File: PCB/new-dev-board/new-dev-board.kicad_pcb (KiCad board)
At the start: 2 copper layers, 185 x 135 mm, 4 parts, among them J1 SIM7600

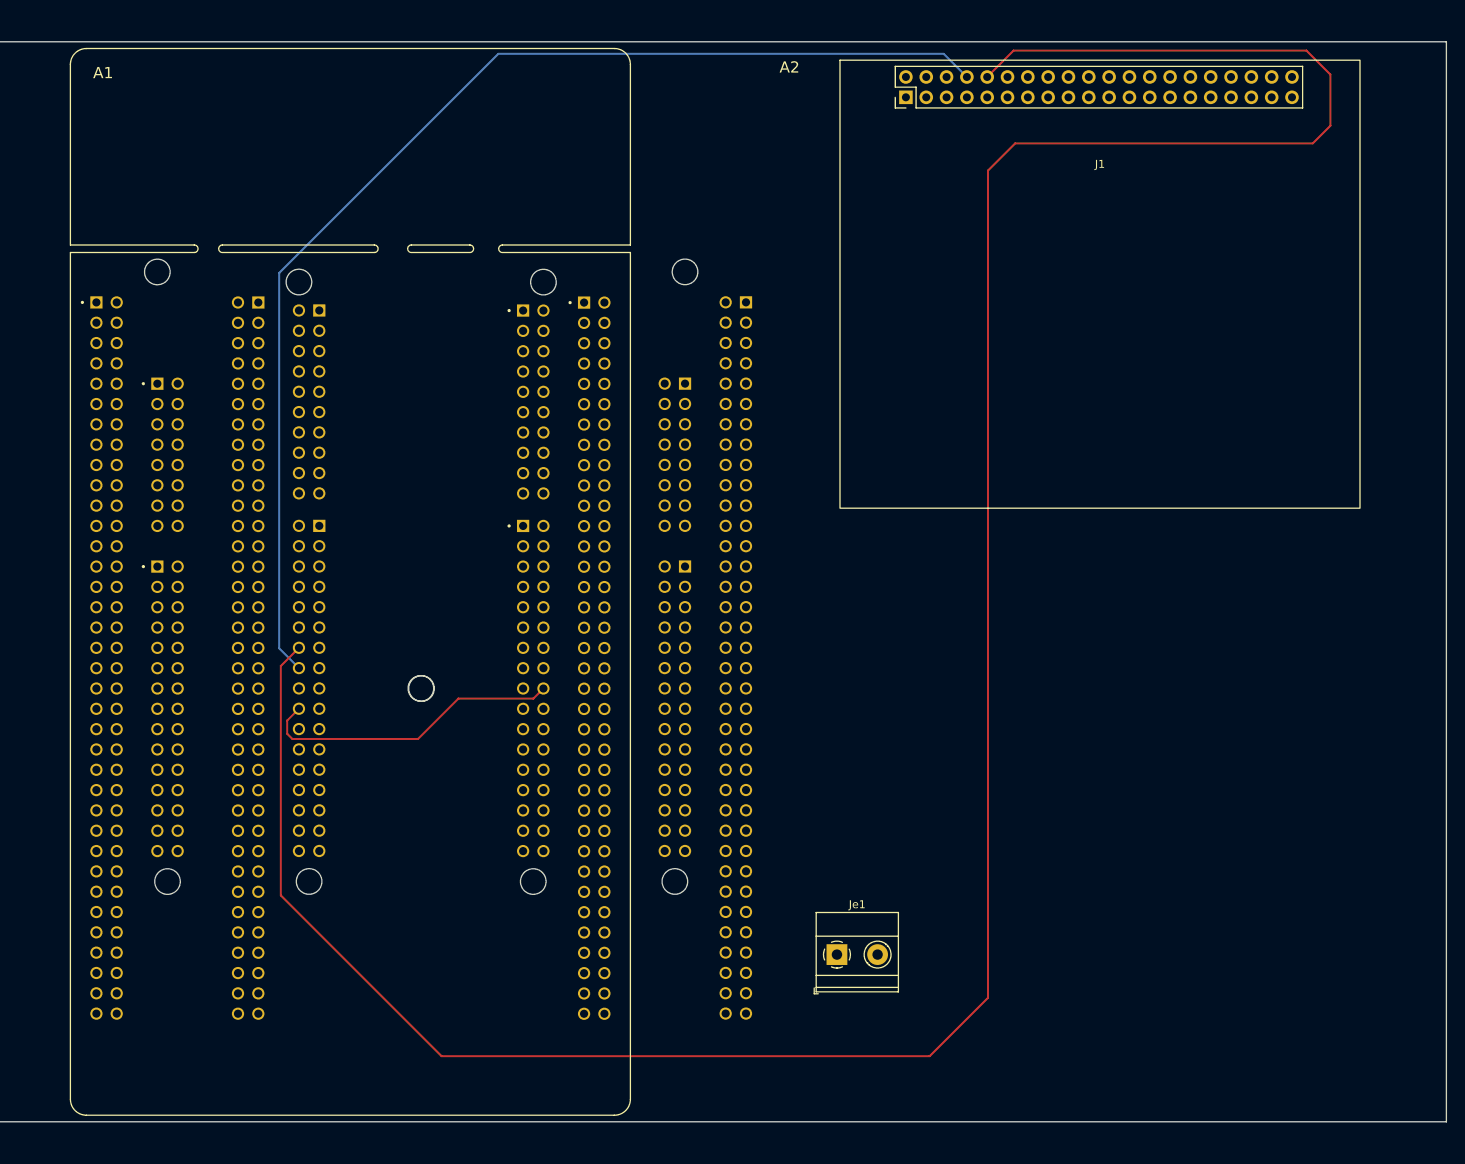
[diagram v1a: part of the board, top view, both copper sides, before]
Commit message: added 2 mount holes
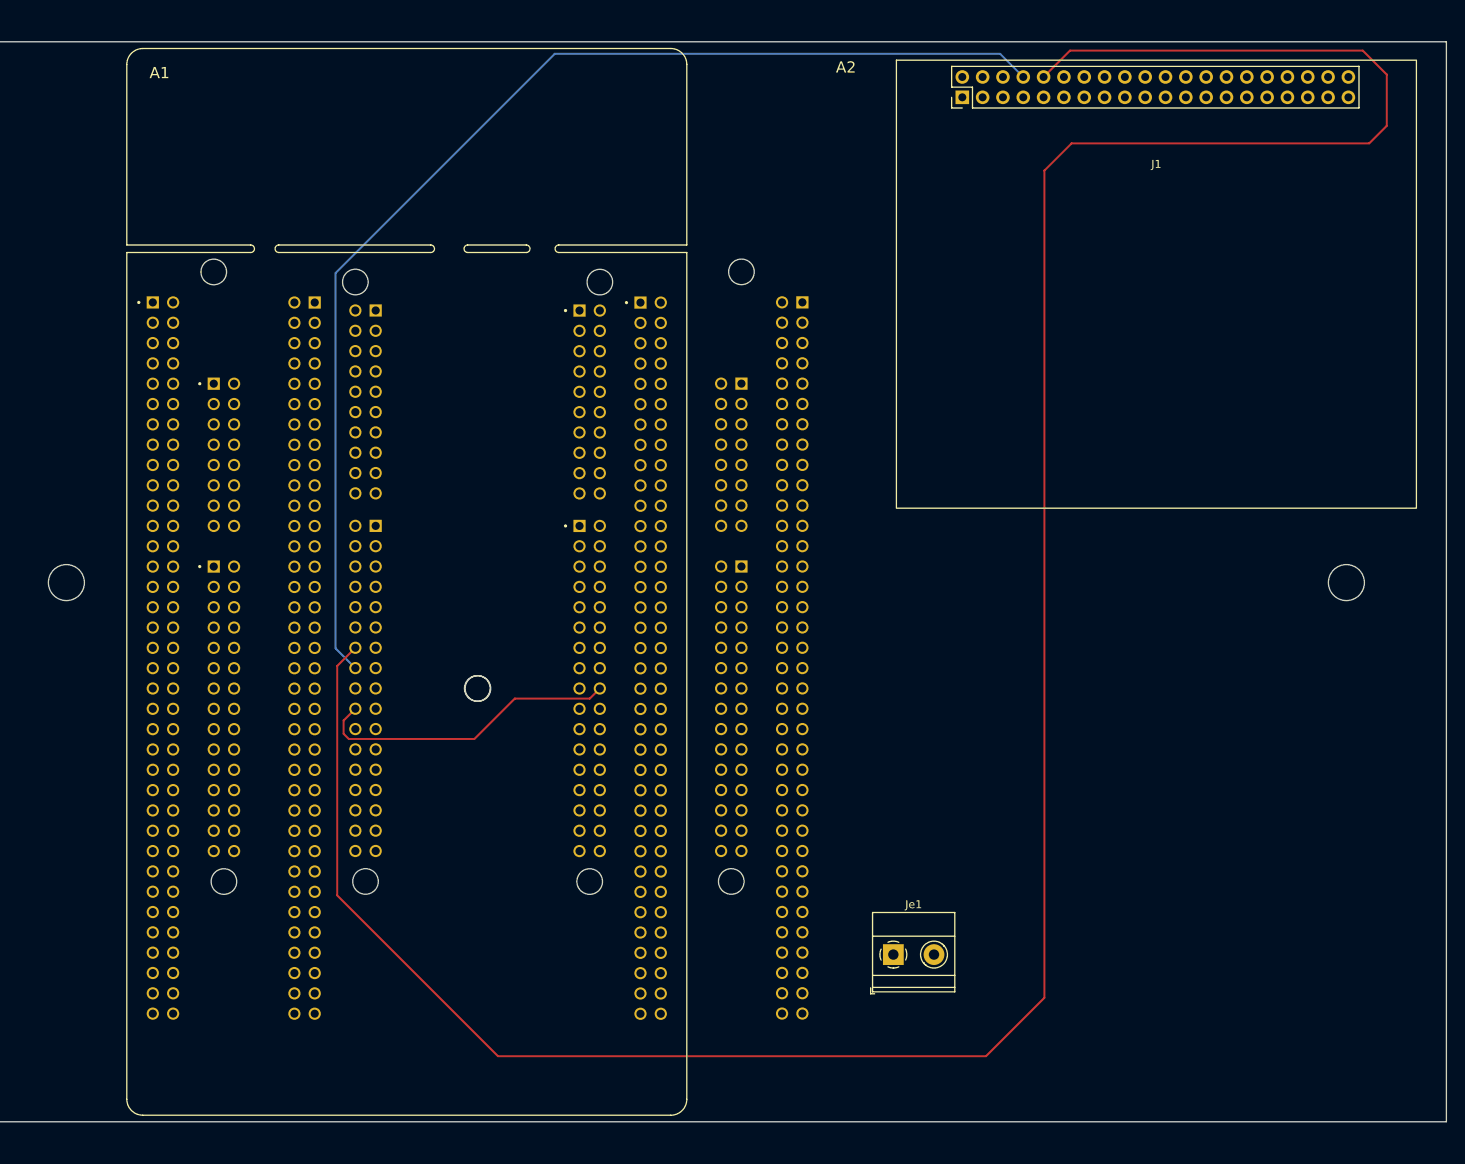
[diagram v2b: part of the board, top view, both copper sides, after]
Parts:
- moved J1 7.05 mm to (201.2, 50.1)
- moved Je1 7.05 mm to (168.4, 133.9)
- moved A1 7.05 mm to (107.5, 87.3)
- moved A2 7.05 mm to (125.2, 87.3)
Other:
- outline, holes or cut-outs redrawn
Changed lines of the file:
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@@
       (drillshape 0)
       (scaleselection 1)
-      (outputdirectory "gerber files/")
+      (outputdirectory "gerber files/first_try/")
     )
   )
@@
   (net 477 "unconnected-(J1-Pin_40-Pad40)")
   (footprint "NUCLEO-F767ZI:SIM7600" (layer "F.Cu")
-    (at 194.2 50.1)
+    (at 201.25 50.1)
     (property "Sheetfile" "new-dev-board.kicad_sch")
     (property "Sheetname" "")
@@
   )
   (footprint "TerminalBlock_Phoenix:TerminalBlock_Phoenix_MKDS-1,5-2-5.08_1x02_P5.08mm_Horizontal" (layer "F.Cu")
-    (at 161.32 133.9)
+    (at 168.37 133.9)
     (descr "Terminal Block Phoenix MKDS-1,5-2-5.08, 2 pins, pitch 5.08mm, size 10.2x9.8mm^2, drill diamater 1.3mm, pad diameter 2.6mm, see http://www.farnell.com/datasheets/100425.pdf, script-generated using https://github.com/pointhi/kicad-footprint-generator/scripts/TerminalBlock_Phoenix")
     (tags "THT Terminal Block Phoenix MKDS-1,5-2-5.08 pitch 5.08mm size 10.2x9.8mm^2 drill 1.3mm pad 2.6mm")
@@
   )
   (footprint "NUCLEO-F767ZI:NUCLEO-F767ZI" (layer "F.Cu")
-    (at 100.5 87.31)
+    (at 107.55 87.31)
     (property "MANUFACTURER" "STMicroelectronics")
     (property "MAXIMUM_PACKAGE_HEIGHT" "N/A")
@@
   )
   (footprint "NUCLEO-F767ZI:NUCLEO-F767ZI" (layer "B.Cu")
-    (at 118.2 87.3 180)
+    (at 125.25 87.3 180)
     (property "MANUFACTURER" "STMicroelectronics")
     (property "MAXIMUM_PACKAGE_HEIGHT" "N/A")
@@
   (gr_rect (start 52.5 19.8) (end 237.5 154.8)
     (stroke (width 0.1) (type default)) (fill none) (layer "Edge.Cuts"))
-  (segment (start 123.37 101.9) (end 114 101.9) (width 0.25) (layer "F.Cu") (net 124))
-  (segment (start 92.6 106.3) (end 92.6 104.64) (width 0.25) (layer "F.Cu") (net 124))
-  (segment (start 124.63 100.64) (end 123.37 101.9) (width 0.25) (layer "F.Cu") (net 124))
-  (segment (start 108.95 106.95) (end 93.25 106.95) (width 0.25) (layer "F.Cu") (net 124))
-  (segment (start 93.25 106.95) (end 92.6 106.3) (width 0.25) (layer "F.Cu") (net 124))
-  (segment (start 92.6 104.64) (end 94.07 103.17) (width 0.25) (layer "F.Cu") (net 124))
-  (segment (start 114 101.9) (end 108.95 106.95) (width 0.25) (layer "F.Cu") (net 124))
-  (segment (start 223 23.9) (end 220 20.9) (width 0.25) (layer "F.Cu") (net 341))
-  (segment (start 223 30.3) (end 223 23.9) (width 0.25) (layer "F.Cu") (net 341))
-  (segment (start 172.9 146.6) (end 180.2 139.3) (width 0.25) (layer "F.Cu") (net 341))
-  (segment (start 220 20.9) (end 183.4 20.9) (width 0.25) (layer "F.Cu") (net 341))
-  (segment (start 91.8 126.5) (end 111.9 146.6) (width 0.25) (layer "F.Cu") (net 341))
-  (segment (start 220.8 32.5) (end 223 30.3) (width 0.25) (layer "F.Cu") (net 341))
-  (segment (start 180.2 35.9) (end 183.6 32.5) (width 0.25) (layer "F.Cu") (net 341))
-  (segment (start 180.2 139.3) (end 180.2 35.9) (width 0.25) (layer "F.Cu") (net 341))
-  (segment (start 94.07 95.55) (end 91.8 97.82) (width 0.25) (layer "F.Cu") (net 341))
-  (segment (start 183.6 32.5) (end 220.8 32.5) (width 0.25) (layer "F.Cu") (net 341))
-  (segment (start 183.4 20.9) (end 180.1 24.2) (width 0.25) (layer "F.Cu") (net 341))
-  (segment (start 111.9 146.6) (end 172.9 146.6) (width 0.25) (layer "F.Cu") (net 341))
-  (segment (start 91.8 97.82) (end 91.8 126.5) (width 0.25) (layer "F.Cu") (net 341))
-  (segment (start 91.6 48.7) (end 91.6 95.62) (width 0.25) (layer "B.Cu") (net 343))
-  (segment (start 91.6 95.62) (end 94.07 98.09) (width 0.25) (layer "B.Cu") (net 343))
-  (segment (start 174.66 21.3) (end 119 21.3) (width 0.25) (layer "B.Cu") (net 343))
-  (segment (start 119 21.3) (end 91.6 48.7) (width 0.25) (layer "B.Cu") (net 343))
-  (segment (start 177.56 24.2) (end 174.66 21.3) (width 0.25) (layer "B.Cu") (net 343))
+  (gr_circle (center 225 87.4) (end 227.25 87.4)
+    (stroke (width 0.1) (type default)) (fill none) (layer "Edge.Cuts"))
+  (gr_circle (center 65 87.4) (end 67.25 87.4)
+    (stroke (width 0.1) (type default)) (fill none) (layer "Edge.Cuts"))
+  (gr_rect (start 51.05 18.6) (end 238.95 156.2)
+    (stroke (width 0.15) (type default)) (fill none) (layer "Margin"))
+  (segment (start 130.42 101.9) (end 121.05 101.9) (width 0.25) (layer "F.Cu") (net 124))
+  (segment (start 99.65 106.3) (end 99.65 104.64) (width 0.25) (layer "F.Cu") (net 124))
+  (segment (start 131.68 100.64) (end 130.42 101.9) (width 0.25) (layer "F.Cu") (net 124))
+  (segment (start 116 106.95) (end 100.3 106.95) (width 0.25) (layer "F.Cu") (net 124))
+  (segment (start 100.3 106.95) (end 99.65 106.3) (width 0.25) (layer "F.Cu") (net 124))
+  (segment (start 99.65 104.64) (end 101.12 103.17) (width 0.25) (layer "F.Cu") (net 124))
+  (segment (start 121.05 101.9) (end 116 106.95) (width 0.25) (layer "F.Cu") (net 124))
+  (segment (start 230.05 23.9) (end 227.05 20.9) (width 0.25) (layer "F.Cu") (net 341))
+  (segment (start 230.05 30.3) (end 230.05 23.9) (width 0.25) (layer "F.Cu") (net 341))
+  (segment (start 179.95 146.6) (end 187.25 139.3) (width 0.25) (layer "F.Cu") (net 341))
+  (segment (start 227.05 20.9) (end 190.45 20.9) (width 0.25) (layer "F.Cu") (net 341))
+  (segment (start 98.85 126.5) (end 118.95 146.6) (width 0.25) (layer "F.Cu") (net 341))
+  (segment (start 227.85 32.5) (end 230.05 30.3) (width 0.25) (layer "F.Cu") (net 341))
+  (segment (start 187.25 35.9) (end 190.65 32.5) (width 0.25) (layer "F.Cu") (net 341))
+  (segment (start 187.25 139.3) (end 187.25 35.9) (width 0.25) (layer "F.Cu") (net 341))
+  (segment (start 101.12 95.55) (end 98.85 97.82) (width 0.25) (layer "F.Cu") (net 341))
+  (segment (start 190.65 32.5) (end 227.85 32.5) (width 0.25) (layer "F.Cu") (net 341))
+  (segment (start 190.45 20.9) (end 187.15 24.2) (width 0.25) (layer "F.Cu") (net 341))
+  (segment (start 118.95 146.6) (end 179.95 146.6) (width 0.25) (layer "F.Cu") (net 341))
+  (segment (start 98.85 97.82) (end 98.85 126.5) (width 0.25) (layer "F.Cu") (net 341))
+  (segment (start 98.65 48.7) (end 98.65 95.62) (width 0.25) (layer "B.Cu") (net 343))
+  (segment (start 98.65 95.62) (end 101.12 98.09) (width 0.25) (layer "B.Cu") (net 343))
+  (segment (start 181.71 21.3) (end 126.05 21.3) (width 0.25) (layer "B.Cu") (net 343))
+  (segment (start 126.05 21.3) (end 98.65 48.7) (width 0.25) (layer "B.Cu") (net 343))
+  (segment (start 184.61 24.2) (end 181.71 21.3) (width 0.25) (layer "B.Cu") (net 343))
   (zone (net 6) (net_name "/TSC_STM/E5V") (layer "F.Cu") (hatch edge 0.5)
     (connect_pads (clearance 0.5))
